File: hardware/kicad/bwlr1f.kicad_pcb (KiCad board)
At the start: 2 copper layers, 39.7 x 22.6 mm, 59 parts, among them J1 Conn_01x02, Q1 PMV32UP, U1 NBM7100ABQX, U2 RAK3172-SIP, U3 ZD24C16A, U4 BME688, U5 TPL5110DDCT

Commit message: finishing
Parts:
- C17: renamed from C14; footprint Capacitor_SMD:C_0402_1005Metric -> Capacitor_SMD:C_0603_1608Metric
- C22, C23: value 100n -> 100nF
- L2: footprint Inductor_SMD:L_1206_3216Metric -> Inductor_SMD:L_0805_2012Metric
- moved L2 0.29 mm to (135.3, 113.4)
- moved C17 0.19 mm to (143.3, 109.8)
- moved C11 0.10 mm to (143.1, 100.0)
- renumbered C12 to C11, C15 to C12, C16 to C13, C19 to C14, C11 to C15, C13 to C16, C20 to C18, C17 to C19, C21 to C20, C18 to C21, L4 to L3, L5 to L4, L3 to L5, R2 to R1, R3 to R2, R7 to R3, R8 to R4, R1 to R5, R4 to R6, R5 to R7, R6 to R8, TP9 to TP7, TP7 to TP8, TP8 to TP9, U2 to U1, U1 to U2
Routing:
- net +3V0: track 95.8 -> 105.6 mm
- net /SCL: track 40.4 -> 38.8 mm
- net /RF: track 3.35 -> 4.18 mm
- net Net-(U1-VFBSMPS): track 8.38 -> 7.78 mm
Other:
- outline, holes or cut-outs redrawn

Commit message: wip: re-route layout
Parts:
- C3, C7: moved to F.Cu
- C5, L1: moved to B.Cu
- moved TP4 15.6 mm to (115.6, 113.3)
- moved TP3 10.5 mm to (120.7, 114.7)
- moved C1 3.79 mm to (135.0, 103.2)
- moved C3 3.14 mm to (135.0, 106.0), turned to 90 degrees
- moved C7 2.82 mm to (136.0, 106.0), turned to 90 degrees
- moved C4 2.81 mm to (136.0, 107.9), turned to 90 degrees
- moved L2 2.77 mm to (135.6, 110.7), turned to -90 degrees
- moved C2 2.57 mm to (135.6, 104.6), turned to 0 degrees
- moved C9 2.04 mm to (133.8, 109.4)
- moved C6 1.93 mm to (136.0, 103.2)
- moved L1 1.73 mm to (135.7, 110.7), turned to 90 degrees
- moved C8 1.71 mm to (135.0, 107.9), turned to 90 degrees
- moved C10 0.84 mm to (133.8, 110.3)
- moved C5 0.66 mm to (136.9, 110.2)
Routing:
- net +3V0: track 105.6 -> 90.6 mm
- net /SWCLK: track 11.8 -> 0.00 mm
- net /BATT+: track 11.5 -> 0.00 mm
- net /SWDIO: track 10.0 -> 0.00 mm
- net Net-(U4-CSB): track 4.18 -> 0.00 mm
- net Net-(U1-VDDMPS): track 4.90 -> 1.68 mm, vias 0 -> 1
- net Net-(U1-VFBSMPS): track 7.78 -> 5.77 mm
- net Net-(U1-VLXSMPS): track 4.70 -> 3.32 mm
- net /SDA: track 38.5 -> 37.3 mm, vias 4 -> 3

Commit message: wip: re-layout
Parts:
- added C25: 1uF, Capacitor_SMD:C_0402_1005Metric, B.Cu at (131.8, 105.6)
- added JP1: OUTPUT_SELECT, Jumper:SolderJumper-3_P1.3mm_Open_RoundedPad1.0x1.5mm, B.Cu at (150.9, 117.7)
- added Q2: PMV32UP, Package_TO_SOT_SMD:SOT-23, F.Cu at (144.1, 117.1)
- added Q3: DMG1012UW, Package_TO_SOT_SMD:SOT-323_SC-70, F.Cu at (140.8, 117.1)
- added R14: 1M, Resistor_SMD:R_0402_1005Metric, F.Cu at (146.6, 117.9)
- added R15: 1M, Resistor_SMD:R_0402_1005Metric, F.Cu at (141.2, 114.7)
- U3: value ZD24C16A -> ZD24C08A
- moved TP8 21.7 mm to (151.2, 101.2)
- moved TP1 17.6 mm to (130.5, 117.7), turned to 0 degrees
- moved R9 15.9 mm to (145.9, 106.0)
- moved TP2 15.5 mm to (130.5, 115.6)
- moved TP4 15.4 mm to (130.5, 109.4), turned to 0 degrees
- moved C24 14.8 mm to (145.3, 108.2)
- moved R10 14.6 mm to (149.2, 105.8), turned to 180 degrees
- moved U5 14.2 mm to (148.0, 108.0)
- moved TP9 11.8 mm to (130.5, 119.8)
- moved TP3 10.3 mm to (130.5, 111.5)
- moved TP7 8.98 mm to (130.5, 113.5)
- moved R11 6.35 mm to (133.1, 107.0)
- moved Q1 5.92 mm to (151.9, 114.5), turned to -90 degrees
- moved C22 4.19 mm to (132.1, 106.0), turned to 0 degrees
- moved C21 3.70 mm to (146.2, 117.6), turned to 180 degrees
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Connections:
- net Net-(U2-VDP) renamed /+VDP
- C21 pad 2: +3V0 -> Net-(JP1-B)
- C24 pad 1: +3V0 -> /BATT+
- Q1 pad 3: Net-(Q1-S) -> Net-(JP1-C)
- R9 pad 1: /DELAY_MDRV -> Net-(Q2-D)
- U1 pad 17: unconnected-(U1-PB6/UART1_TX-Pad17) -> /START
- U1 pad 18: unconnected-(U1-PB7/UART1_RX-Pad18) -> /RDY
- U1 pad 19: /RDY -> unconnected-(U1-PB8-Pad19)
- U1 pad 20: /START -> unconnected-(U1-PB9-Pad20)
- U2 pad 14: Net-(Q1-S) -> Net-(JP1-B)
- U2 pad 9: Net-(Q1-S) -> Net-(JP1-B)
- U5 pad 1: +3V0 -> /BATT+
- U5 pad 3: /DELAY_MDRV -> Net-(Q2-D)
- U5 pad 6: +3V0 -> /BATT+
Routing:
- net /BATT+: track 0.00 -> 38.2 mm, vias 0 -> 4
- net /SWCLK: track 0.00 -> 21.2 mm, vias 0 -> 2
- net /SWDIO: track 0.00 -> 21.2 mm, vias 0 -> 2
- net /RX2: track 7.16 -> 27.1 mm
- net /TX2: track 7.23 -> 26.9 mm
- net Net-(JP1-B): track 0.00 -> 18.5 mm, vias 0 -> 2
- net Net-(Q2-D): track 0.00 -> 18.0 mm, vias 0 -> 2
- net Net-(Q1-S): track 15.1 -> 0.00 mm, vias 2 -> 0
- net /+VDP: track 9.83 -> 20.9 mm, vias 2 -> 0
- net /START: track 12.0 -> 2.82 mm
- net /SDA: track 37.3 -> 45.5 mm
- net /DONE: track 8.04 -> 16.2 mm, vias 1 -> 2
- net +3V0: track 90.6 -> 84.2 mm, vias 8 -> 5
- net Net-(Q2-G): track 0.00 -> 5.30 mm
- net Net-(U1-VDDMPS): track 1.68 -> 5.71 mm
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- added copper zone on In1.Cu, net (none)
- added copper zone on In2.Cu, net (none)
- added copper zone on In1.Cu, net GND
- added copper zone on In2.Cu, net GND
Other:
- copper layers 2 -> 4
- board text added: "+3V0"
- board text added: "BATTERY"
- board text added: "CLK"
- board text added: "DIO"
- board text removed: "+3V3"
- board text removed: "BATT"
- board text removed: "SWCLK"
- board text removed: "SWDIO"

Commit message: wip: initial pcb prod
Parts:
- added G***: LOGO, bwlr1f:TeapotLogo4mm, F.Cu at (154.0, 117.0)
- added G***: LOGO, bwlr1f:TeapotLogo4mm, B.Cu at (133.1, 109.3)
- C16: footprint Teapot:CAPPM7362X200N -> Capacitor_Tantalum_SMD:CP_EIA-7343-40_Kemet-Y
- E1: footprint Teapot:XDCR_ANT-915-USP410 -> bwlr1f:XDCR_ANT-915-USP410
- J1: footprint Teapot:Battery_Pad -> bwlr1f:Battery_Pad
- L5: footprint Teapot:74404042150 -> bwlr1f:74404042150
- U1: footprint Teapot:RAK3172-SiP_LGA75 -> bwlr1f:RAK3172-SiP_LGA75
- U2: footprint Teapot:NBM7100ABQX -> bwlr1f:NBM7100ABQX
- U4: footprint Teapot:BME680-PSON80P300X300X100-8N -> bwlr1f:BME680-PSON80P300X300X100-8N
- U5: value TPL5110DDCT -> TPL5110; footprint Teapot:SOT95P280X110-6N -> Package_TO_SOT_SMD:SOT-23-6
- moved C16 0.89 mm to (139.9, 106.7)
- moved U1 0.16 mm to (143.8, 107.2)
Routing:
- net +3V0: track 84.2 -> 86.5 mm
- net Net-(U2-CAP): track 6.02 -> 4.62 mm
- net Net-(U2-LX1): track 6.16 -> 6.86 mm
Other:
- board text added: "BWLR1F"
- board text added: "EEPROM"
- board text added: "OUTPUT SELECT"
- board text added: "POWER GATE"
- board text added: "PROGRAM"
- board text added: "PWR REG"
- board text added: "REVISION 1"
- board text added: "Teapotlabs"

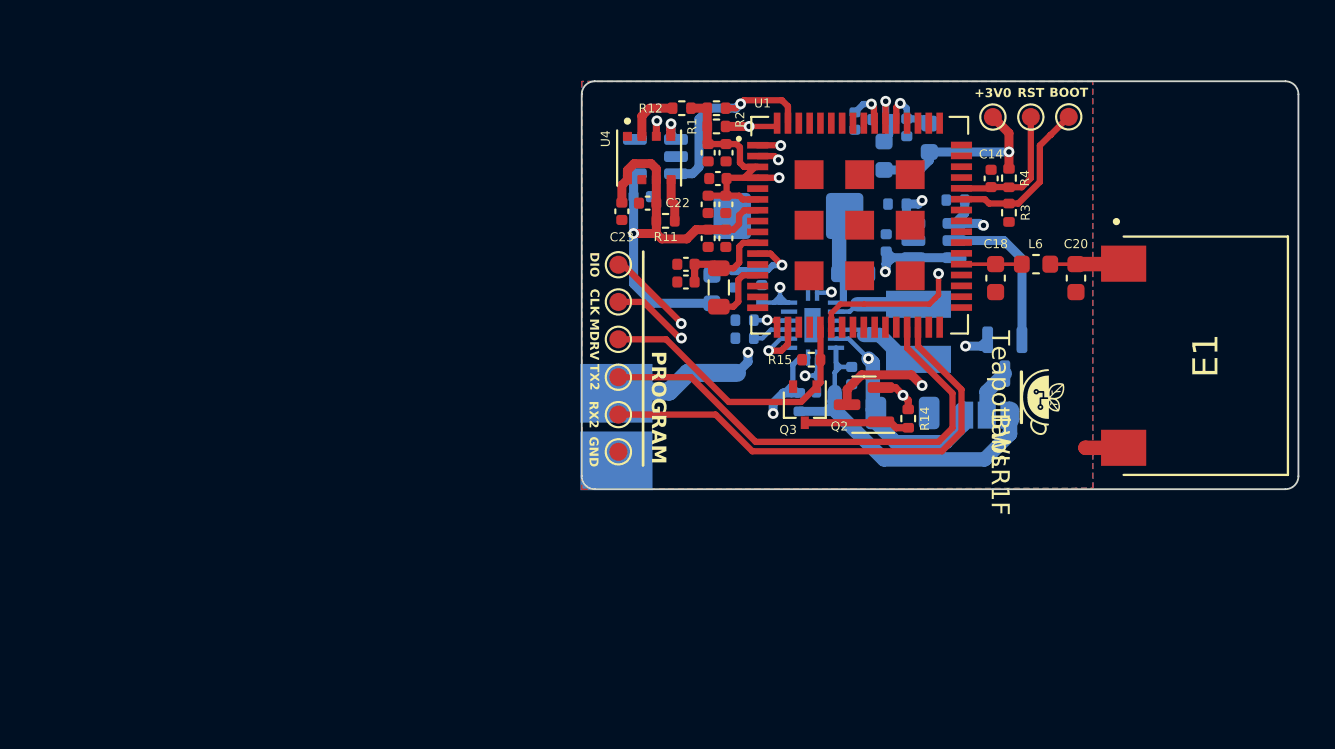
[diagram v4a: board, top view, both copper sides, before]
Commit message: add battery pack
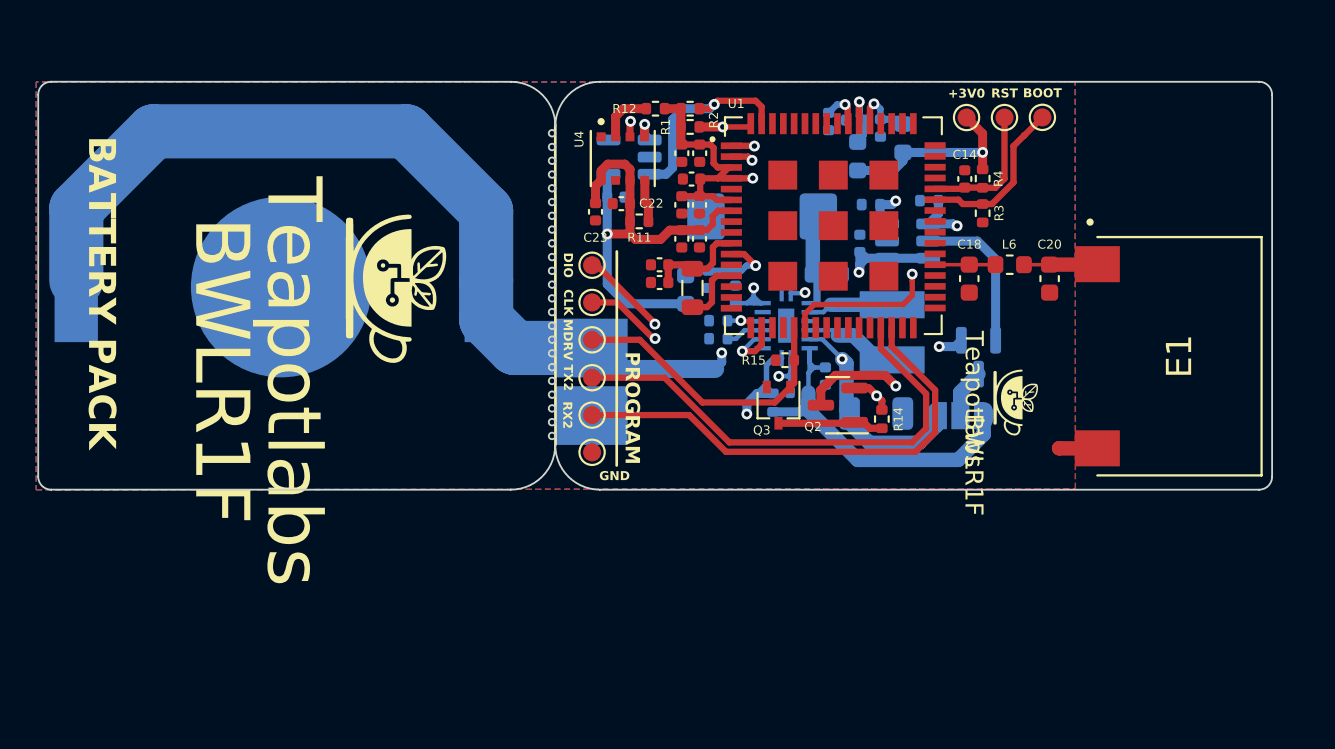
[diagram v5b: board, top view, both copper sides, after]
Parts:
- added BT1: Battery_Cell, bwlr1f:BAT-SMD_MY-2032-12, B.Cu at (111.8, 110.6)
- added G***: LOGO, bwlr1f:TeapotLogo, F.Cu at (118.2, 110.2)
- moved J1 2.86 mm to (128.6, 115.9)
- moved C10 1.46 mm to (132.8, 110.4)
- moved C13 1.46 mm to (145.0, 101.8)
- moved C15 1.46 mm to (137.0, 111.0)
- moved C17 1.46 mm to (142.0, 109.9)
- moved C20 1.46 mm to (154.4, 110.2)
- moved C21 1.46 mm to (144.8, 117.6)
- moved C22 1.46 mm to (130.7, 106.0)
- moved C23 1.46 mm to (129.2, 106.5)
- moved C24 1.46 mm to (143.9, 108.2)
- moved C4 1.46 mm to (135.0, 108.0)
- moved C5 1.46 mm to (135.5, 110.2)
- moved C6 1.46 mm to (135.0, 103.2)
- moved C7 1.46 mm to (135.0, 106.1)
- moved C9 1.46 mm to (132.8, 109.4)
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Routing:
- net /BATT+: track 38.2 -> 81.8 mm
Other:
- board size 39.7 x 22.6 mm -> 68.3 x 22.6 mm
- board text added: "BATTERY PACK"

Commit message: first production file revision 1
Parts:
- removed the G*** at (118.2, 110.2)
- added BT2: Battery_Cell, bwlr1f:BAT-SMD_MY-2032-12, F.Cu at (115.9, 110.7)
- added TP10: BATT+, TestPoint:TestPoint_Pad_D1.0mm, F.Cu at (134.0, 119.8)
- C1, C3: value 4.7uF -> 4u7
- C10, C11, C14, C22, C23, C24, C5, C6, C7, C8: value 100nF -> 100n
- C12, C13, C15, C19, C2, C25: value 1uF -> 1u
- C16: value 470uF -> 470u
- C17: value 10uF -> 10u
- C21: value 22uF -> 22u
- C4: value 1uF -> 4u7
- C9: value 470nF -> 470n
- L1, L3, L4: footprint Inductor_SMD:L_0603_1608Metric -> Inductor_SMD:L_0402_1005Metric
- L2, L5: value 15uH -> 15u
- R1, R2: value 4.7K -> 4K7
- R9: value 16.9K -> 16K9
- moved BT1 4.13 mm to (116.0, 110.7), turned to 90 degrees
- moved L4 1.35 mm to (145.0, 101.9)
- moved R15 1.02 mm to (140.7, 114.6), turned to 0 degrees
- moved C13 1.00 mm to (146.0, 101.8)
- moved L3 0.62 mm to (144.0, 102.8)
- moved L1 0.60 mm to (134.5, 110.2)
- turned C19 to 90 degrees
- turned C24 to -90 degrees
- turned Q1 to 90 degrees
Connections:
- C19 pad 1: /+VDP -> GND
- C19 pad 2: GND -> /+VDP
- C24 pad 1: /BATT+ -> GND
- C24 pad 2: GND -> /BATT+
- Q1 pad 1: +3V0 -> /DRV
- Q1 pad 2: /DRV -> Net-(JP1-C)
- Q1 pad 3: Net-(JP1-C) -> +3V0
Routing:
- net /BATT+: track 81.8 -> 107.2 mm, vias 4 -> 21
- net +3V0: track 86.5 -> 89.7 mm
- net /+VDP: track 20.9 -> 23.8 mm
- net Net-(U2-LX2): track 4.74 -> 7.60 mm
- net Net-(U2-LX1): track 6.86 -> 9.39 mm
- net GND: track 2.12 -> 0.00 mm, vias 0 -> 69
- net /DRV: track 8.62 -> 10.5 mm
- net /TX2: track 26.9 -> 27.5 mm
- net /RX2: track 27.1 -> 27.6 mm
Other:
- board size 68.3 x 22.6 mm -> 61.2 x 26.1 mm
- board text added: "BATT+"
- board text added: "PCB3D_BR_bwlr1f"
- board text added: "PCB3D_TL_bwlr1f"
- board text removed: "BATTERY PACK"
